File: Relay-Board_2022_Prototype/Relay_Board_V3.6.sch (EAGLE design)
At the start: 61 parts

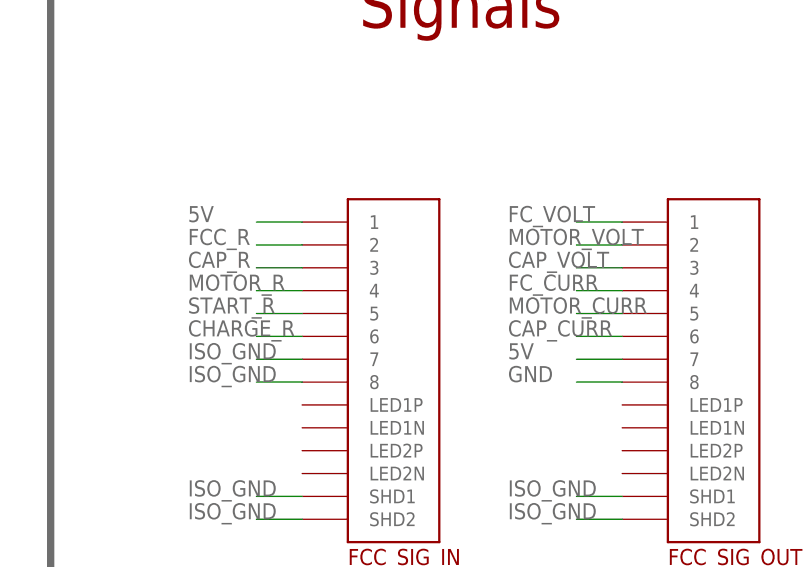
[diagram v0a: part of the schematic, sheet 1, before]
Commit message: Removed 5V from signal connections
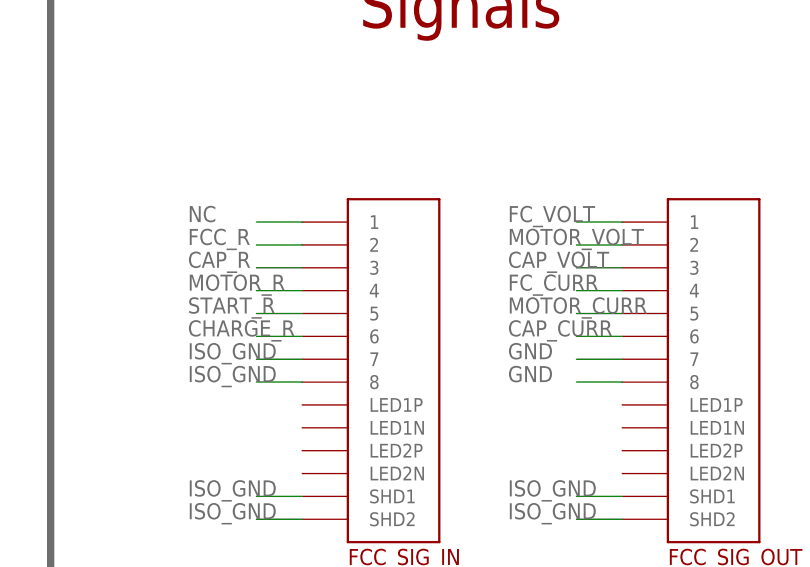
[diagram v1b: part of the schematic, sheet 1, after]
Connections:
- new net NC: FCC_SIG_IN.1
- net 5V: no longer FCC_SIG_IN.1, FCC_SIG_OUT.7
- net GND: now also FCC_SIG_OUT.7
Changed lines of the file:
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@@
-</segment>
-<segment>
-<pinref part="FCC_SIG_IN" gate="G$1" pin="1"/>
-<wire x1="157.48" y1="88.9" x2="152.4" y2="88.9" width="0.1524" layer="91"/>
-<label x="144.78" y="88.9" size="1.778" layer="95"/>
-</segment>
-<segment>
-<pinref part="FCC_SIG_OUT" gate="G$1" pin="7"/>
-<wire x1="187.96" y1="73.66" x2="193.04" y2="73.66" width="0.1524" layer="91"/>
-<label x="180.34" y="73.66" size="1.778" layer="95"/>
 </segment>
 <segment>
@@
 <label x="182.88" y="-63.5" size="1.778" layer="95"/>
 </segment>
+<segment>
+<pinref part="FCC_SIG_OUT" gate="G$1" pin="7"/>
+<wire x1="193.04" y1="73.66" x2="187.96" y2="73.66" width="0.1524" layer="91"/>
+<label x="180.34" y="73.66" size="1.778" layer="95"/>
+</segment>
 </net>
 <net name="FC_CURR" class="0">
@@
 </segment>
 </net>
+<net name="NC" class="0">
+<segment>
+<pinref part="FCC_SIG_IN" gate="G$1" pin="1"/>
+<wire x1="157.48" y1="88.9" x2="152.4" y2="88.9" width="0.1524" layer="91"/>
+<label x="144.78" y="88.9" size="1.778" layer="95"/>
+</segment>
+</net>

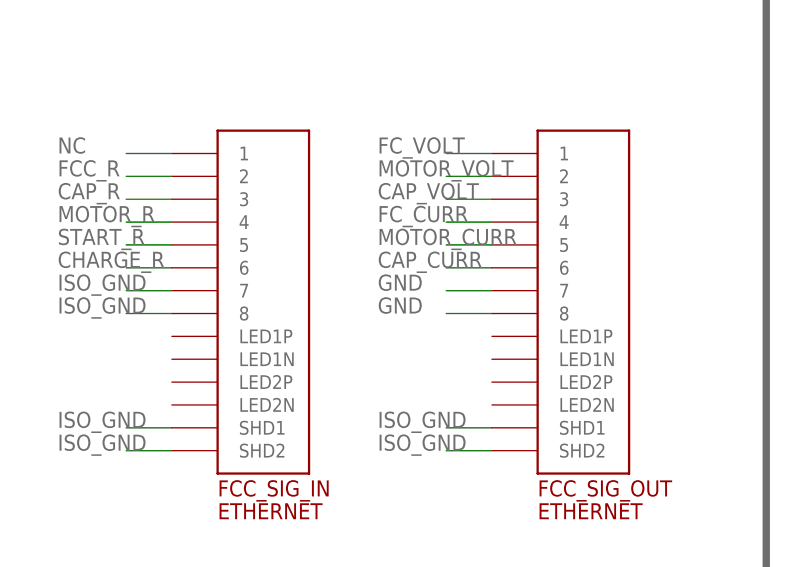
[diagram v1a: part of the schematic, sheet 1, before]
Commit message: Added label for FC Power Board Relay
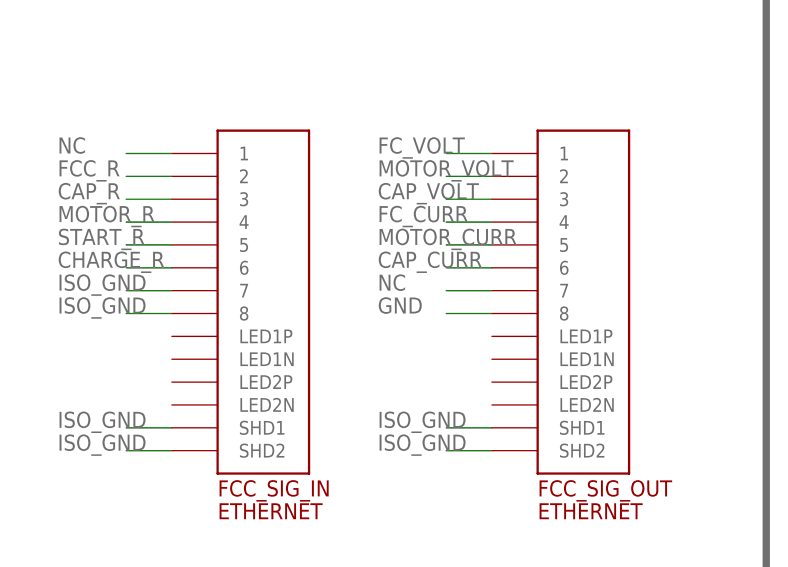
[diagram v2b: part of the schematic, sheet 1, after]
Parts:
- renumbered U$22 to FC_POWER_BOARD_RELAY
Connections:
- net GND: no longer FCC_SIG_OUT.7
- net NC: now also FCC_SIG_OUT.7
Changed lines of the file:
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@@
 <part name="R6" library="Resistor" deviceset="R-US_" device="R0805" value="10.5k (0.1%)"/>
 <part name="R7" library="Resistor" deviceset="R-US_" device="R0805" value="775 (0.1%)"/>
-<part name="U$22" library="Relay_CPC1907B" deviceset="RELAY-CPC1907B" device=""/>
+<part name="FC_POWER_BOARD_RELAY" library="Relay_CPC1907B" deviceset="RELAY-CPC1907B" device=""/>
 <part name="FC.POS" library="Connector 732-3204" deviceset="732-3204-ND_CONNECTOR" device=""/>
 <part name="FC.GND" library="Connector 732-3204" deviceset="732-3204-ND_CONNECTOR" device=""/>
@@
 <attribute name="VALUE" x="85.09" y="52.578" size="1.778" layer="96"/>
 </instance>
-<instance part="U$22" gate="G$1" x="66.04" y="-43.18" smashed="yes" rot="R180"/>
+<instance part="FC_POWER_BOARD_RELAY" gate="G$1" x="66.04" y="-43.18" smashed="yes" rot="R180"/>
 <instance part="FC.POS" gate="G$1" x="-106.68" y="99.06" smashed="yes"/>
 <instance part="FC.GND" gate="G$1" x="-106.68" y="88.9" smashed="yes"/>
@@
 </segment>
 <segment>
-<pinref part="U$22" gate="G$1" pin="LED-"/>
+<pinref part="FC_POWER_BOARD_RELAY" gate="G$1" pin="LED-"/>
 <wire x1="73.66" y1="-53.34" x2="48.26" y2="-53.34" width="0.1524" layer="91"/>
 <label x="43.18" y="-53.975" size="1.778" layer="95"/>
@@
 <label x="182.88" y="-63.5" size="1.778" layer="95"/>
 </segment>
-<segment>
-<pinref part="FCC_SIG_OUT" gate="G$1" pin="7"/>
-<wire x1="193.04" y1="73.66" x2="187.96" y2="73.66" width="0.1524" layer="91"/>
-<label x="180.34" y="73.66" size="1.778" layer="95"/>
-</segment>
 </net>
 <net name="FC_CURR" class="0">
@@
 <net name="FCC_R" class="0">
 <segment>
-<pinref part="U$22" gate="G$1" pin="LED+"/>
+<pinref part="FC_POWER_BOARD_RELAY" gate="G$1" pin="LED+"/>
 <wire x1="73.66" y1="-58.42" x2="48.26" y2="-58.42" width="0.1524" layer="91"/>
 <label x="40.005" y="-59.055" size="1.778" layer="95"/>
@@
 <net name="FC_POS" class="0">
 <segment>
-<pinref part="U$22" gate="G$1" pin="7"/>
+<pinref part="FC_POWER_BOARD_RELAY" gate="G$1" pin="7"/>
 <wire x1="73.66" y1="-38.1" x2="60.96" y2="-38.1" width="0.1524" layer="91"/>
-<pinref part="U$22" gate="G$1" pin="8"/>
+<pinref part="FC_POWER_BOARD_RELAY" gate="G$1" pin="8"/>
 <wire x1="73.66" y1="-33.02" x2="60.96" y2="-33.02" width="0.1524" layer="91"/>
 <wire x1="60.96" y1="-38.1" x2="60.96" y2="-33.02" width="0.1524" layer="91"/>
@@
 </segment>
 <segment>
-<pinref part="U$22" gate="G$1" pin="5"/>
+<pinref part="FC_POWER_BOARD_RELAY" gate="G$1" pin="5"/>
 <wire x1="73.66" y1="-48.26" x2="60.96" y2="-48.26" width="0.1524" layer="91"/>
-<pinref part="U$22" gate="G$1" pin="6"/>
+<pinref part="FC_POWER_BOARD_RELAY" gate="G$1" pin="6"/>
 <wire x1="73.66" y1="-43.18" x2="60.96" y2="-43.18" width="0.1524" layer="91"/>
 <wire x1="60.96" y1="-48.26" x2="60.96" y2="-43.18" width="0.1524" layer="91"/>
@@
 <label x="144.78" y="88.9" size="1.778" layer="95"/>
 </segment>
-</net>
+<segment>
+<pinref part="FCC_SIG_OUT" gate="G$1" pin="7"/>
+<wire x1="193.04" y1="73.66" x2="187.96" y2="73.66" width="0.1524" layer="91"/>
+<label x="180.34" y="73.66" size="1.778" layer="95"/>
+</segment>
+</net>

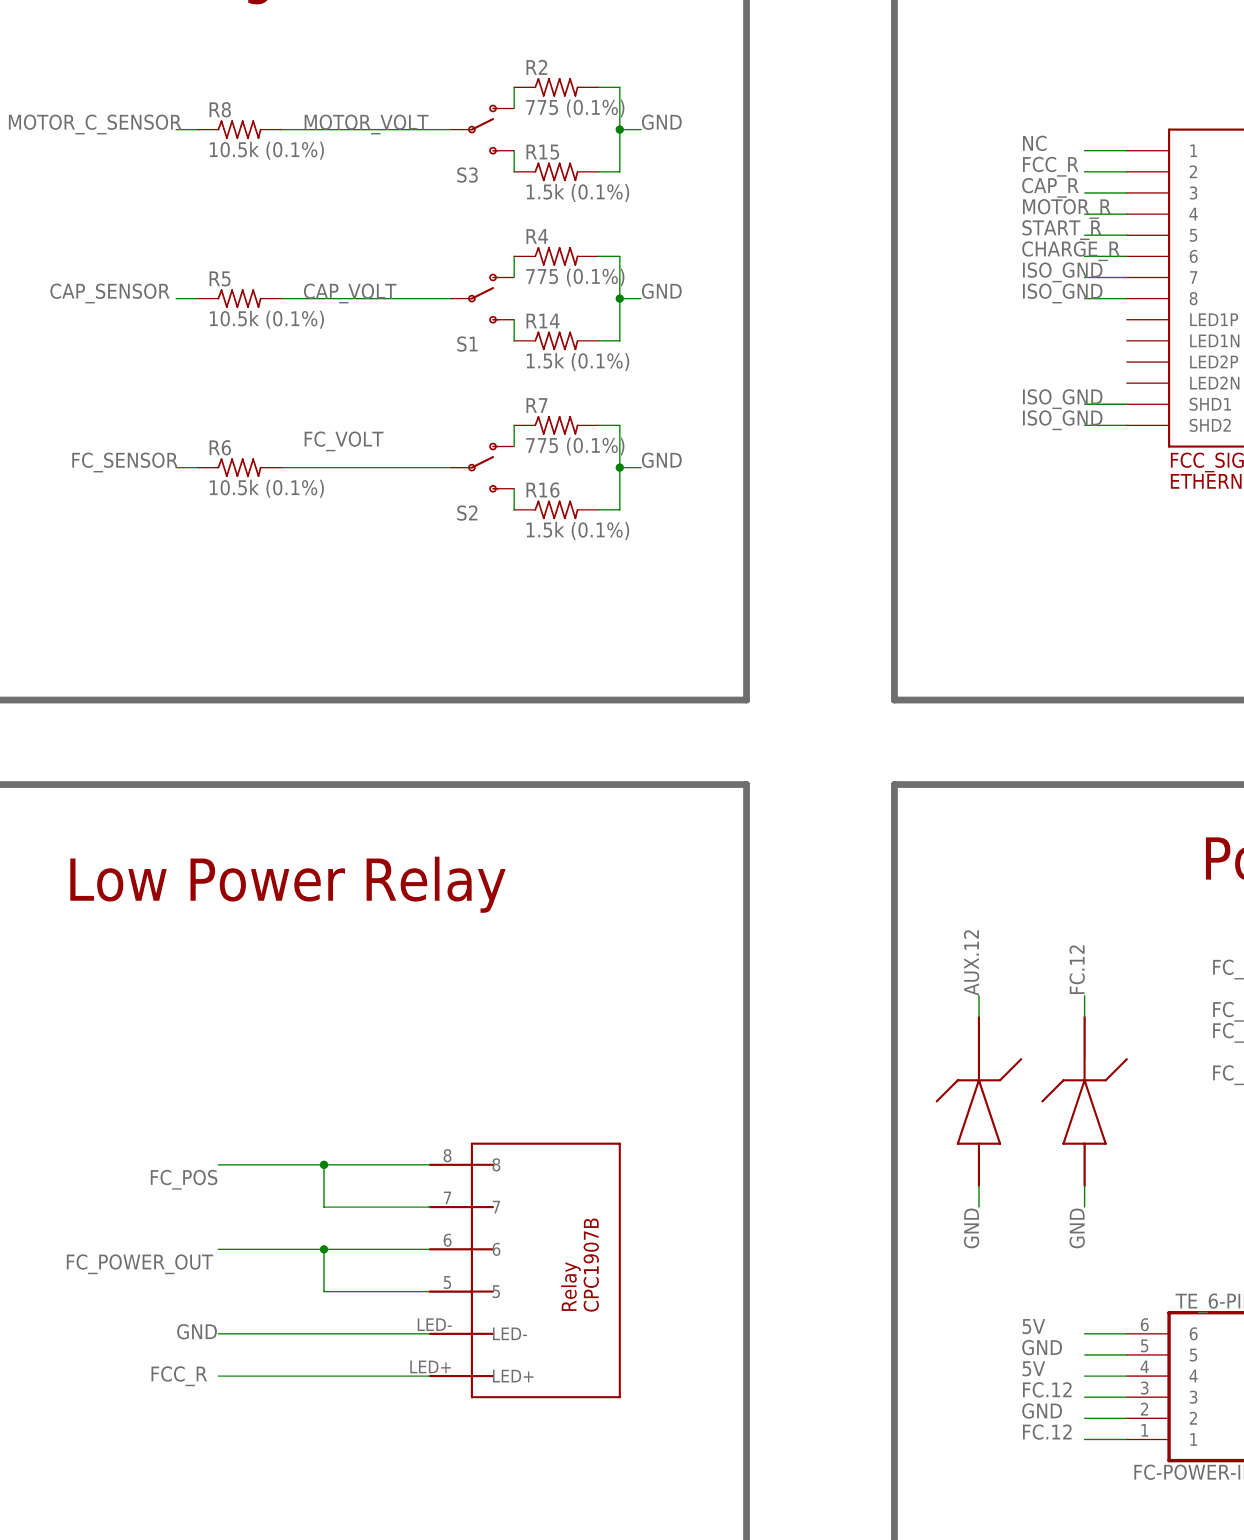
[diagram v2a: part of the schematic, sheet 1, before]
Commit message: Renamed FC Relay net
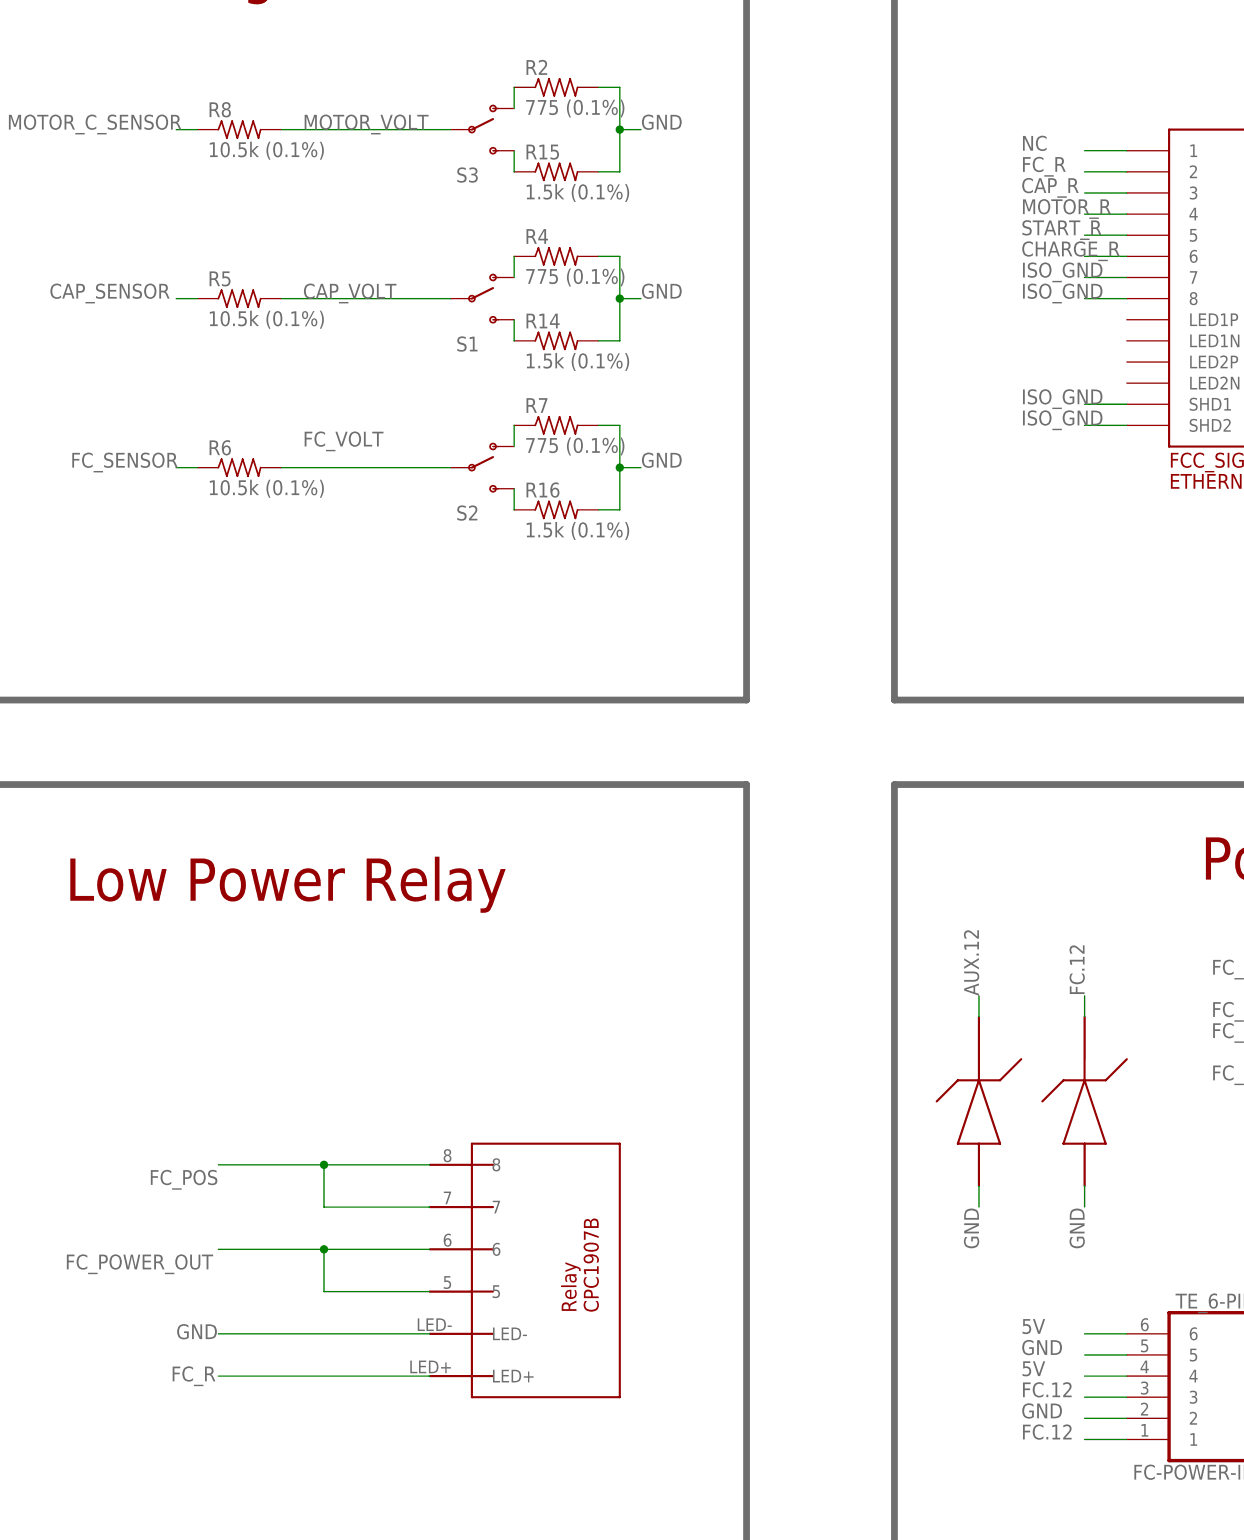
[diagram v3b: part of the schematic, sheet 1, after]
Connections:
- net FCC_R renamed FC_R
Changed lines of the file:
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@@
-</segment>
-</net>
-<net name="FCC_R" class="0">
-<segment>
-<pinref part="FC_POWER_BOARD_RELAY" gate="G$1" pin="LED+"/>
-<wire x1="73.66" y1="-58.42" x2="48.26" y2="-58.42" width="0.1524" layer="91"/>
-<label x="40.005" y="-59.055" size="1.778" layer="95"/>
-</segment>
-<segment>
-<pinref part="FCC_SIG_IN" gate="G$1" pin="2"/>
-<wire x1="152.4" y1="86.36" x2="157.48" y2="86.36" width="0.1524" layer="91"/>
-<label x="144.78" y="86.36" size="1.778" layer="95"/>
 </segment>
 </net>
@@
 </segment>
 </net>
+<net name="FC_R" class="0">
+<segment>
+<pinref part="FC_POWER_BOARD_RELAY" gate="G$1" pin="LED+"/>
+<wire x1="73.66" y1="-58.42" x2="48.26" y2="-58.42" width="0.1524" layer="91"/>
+<label x="42.545" y="-59.055" size="1.778" layer="95"/>
+</segment>
+<segment>
+<pinref part="FCC_SIG_IN" gate="G$1" pin="2"/>
+<wire x1="152.4" y1="86.36" x2="157.48" y2="86.36" width="0.1524" layer="91"/>
+<label x="144.78" y="86.36" size="1.778" layer="95"/>
+</segment>
+</net>
